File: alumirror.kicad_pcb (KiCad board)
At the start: 2 copper layers, 139.7 x 88.9 mm, 96 parts, among them J1 USB_C_Receptacle_USB2.0_16P_2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, J2 USB_C_Receptacle_USB2.0_16P_2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, J3 USB_C_Receptacle_USB2.0_16P_2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, J4 USB_C_Receptacle_USB2.0_16P_2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, K00 PG1350, K01 PG1350, K02 PG1350, K03 PG1350, K04 PG1350, K05 PG1350, K10 PG1350, K11 PG1350, K12 PG1350, K13 PG1350, K14 PG1350, K15 PG1350, K20 PG1350, K21 PG1350, K22 PG1350, K23 PG1350, K24 PG1350, K25 PG1350_1½U, K30 PG1350_1½U, K31 PG1350/SKQUCAA010, SW1 BOOT, U1 CH552T, U2 CH552T, U3 USBLC6-2P6, U4 USBLC6-2P6, U5 USBLC6-2P6, U6 USBLC6-2P6

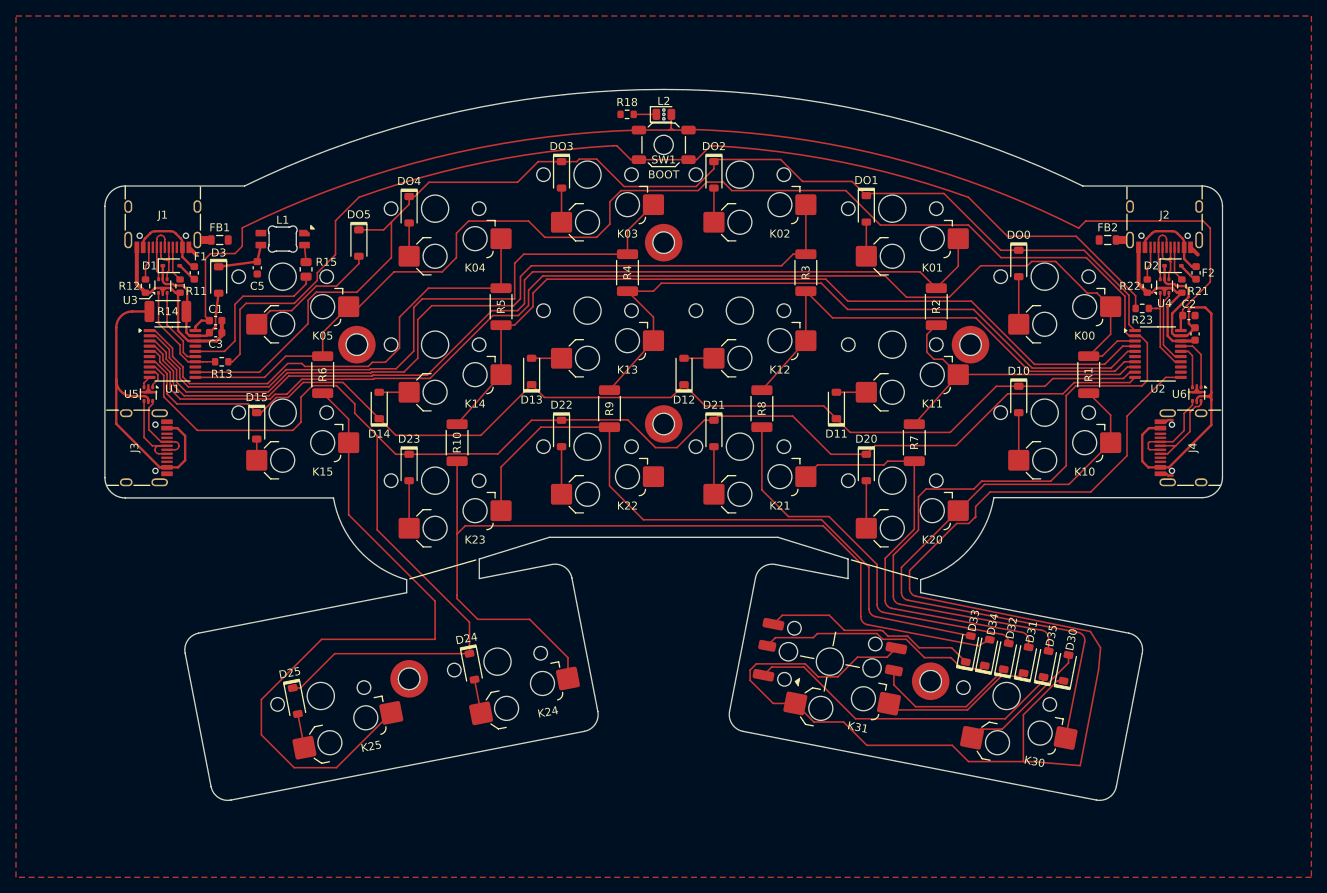
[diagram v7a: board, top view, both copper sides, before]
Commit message: Adjust component locations
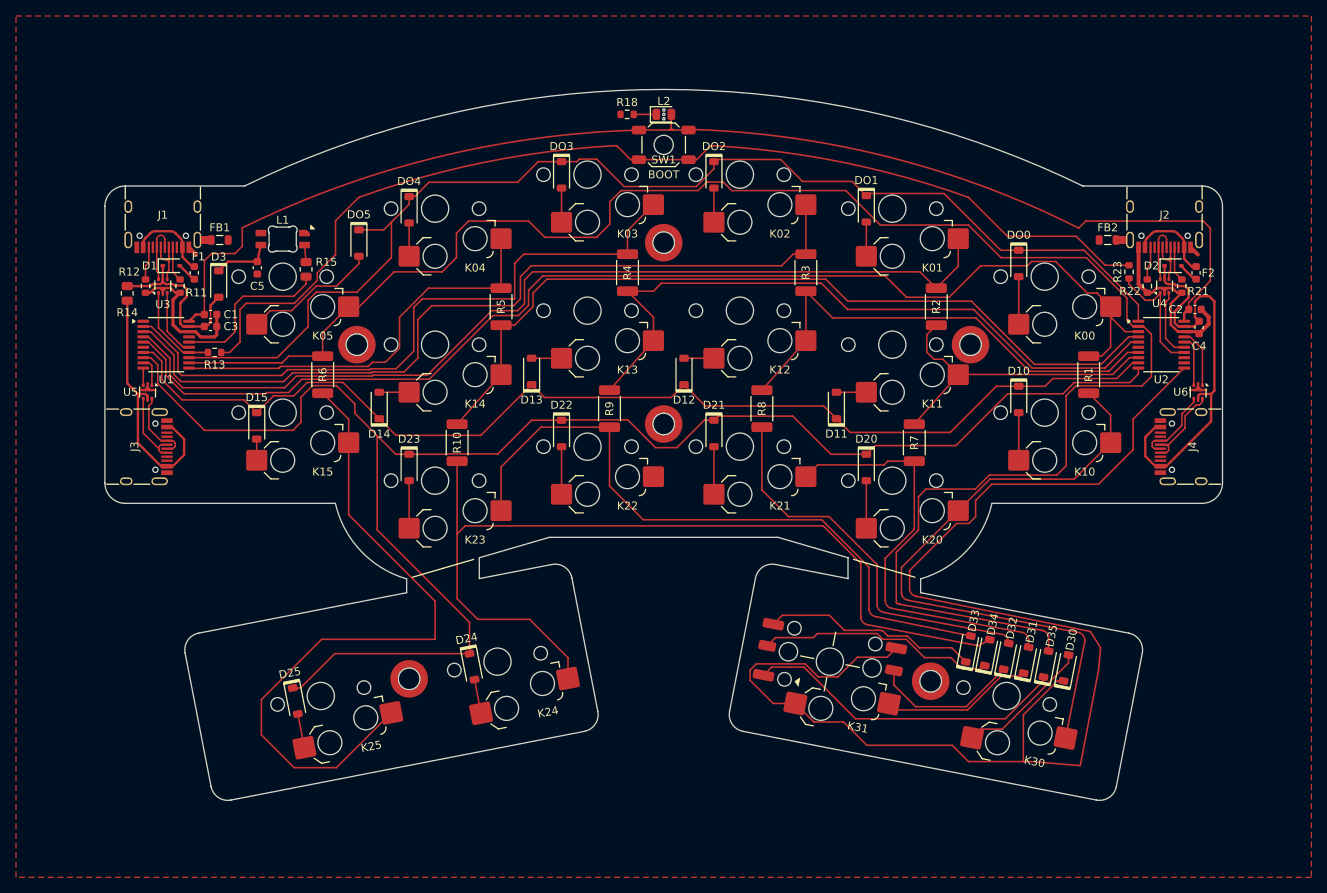
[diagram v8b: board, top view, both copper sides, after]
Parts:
- R14: footprint Resistor_SMD:R_2010_5025Metric -> Resistor_SMD:R_0805_2012Metric
- moved R14 5.56 mm to (85.3, 54.5), turned to -90 degrees
- moved R23 4.86 mm to (210.6, 51.8), turned to 90 degrees
- moved R13 1.46 mm to (96.3, 61.9)
- moved U1 1.41 mm to (90.2, 60.9)
- moved NT2 1.32 mm to (213.1, 55.4)
- moved U2 1.24 mm to (214.6, 60.9)
- moved NT1 1.22 mm to (94.4, 61.9)
- moved C2 1.08 mm to (218.8, 56.5)
- moved C3 1.01 mm to (95.8, 58.6)
- moved C1 0.99 mm to (95.8, 57.1)
- moved C4 0.96 mm to (219.3, 58.8)
- moved D3 0.51 mm to (96.8, 53.3)
- moved U6 0.32 mm to (219.2, 66.8)
- moved U5 0.29 mm to (87.9, 66.8)
- moved J3 0.14 mm to (86.3, 73.7)
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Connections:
- U1 pad 1: Col4L -> unconnected-(U1-P3.2-Pad1)
- U1 pad 11: Col5 -> Col4L
- U1 pad 12: Row0 -> Col5
- U1 pad 13: unconnected-(U1-P3.5-Pad13) -> Row0
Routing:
- net Col4L: track 61.9 -> 51.6 mm
- net GND: track 51.0 -> 42.0 mm
- net VCC_L': track 40.3 -> 32.4 mm
- net BOOT: track 72.8 -> 68.3 mm
- net Net-(NT2-Pad2): track 0.00 -> 3.58 mm
- net VCC_L: track 19.2 -> 22.3 mm
- net VCC_R: track 55.1 -> 52.4 mm
- net +3V3: track 56.8 -> 54.4 mm
- net Row2: track 203.3 -> 205.5 mm
- net Row1: track 141.3 -> 143.2 mm
- net USB_L-: track 10.0 -> 8.36 mm
- net RX_PL: track 11.4 -> 9.77 mm
- net Row0: track 152.0 -> 150.9 mm
- net Net-(D31-K): track 19.1 -> 18.0 mm
- net TX_PR: track 11.1 -> 10.2 mm
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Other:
- outline, holes or cut-outs redrawn
